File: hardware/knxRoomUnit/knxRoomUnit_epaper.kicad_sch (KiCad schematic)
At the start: 24 parts, among them P1 ePaper, P2 ePaper FL, Q3 SI1308

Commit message: Initial hardware commit
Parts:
- R30: renamed from R26; footprint Resistor_SMD:R_0402_1005Metric -> Resistor_SMD:R_0603_1608Metric
- R31: renamed from R27; footprint Resistor_SMD:R_0402_1005Metric -> Resistor_SMD:R_0603_1608Metric
- renumbered C24 to C20, C25 to C22, C20 to C23, C26 to C24, C27 to C25, C28 to C26, C22 to C27, C29 to C28, C23 to C29, P2 to P1, P1 to P2, R28 to R27, R29 to R28, R25 to R29

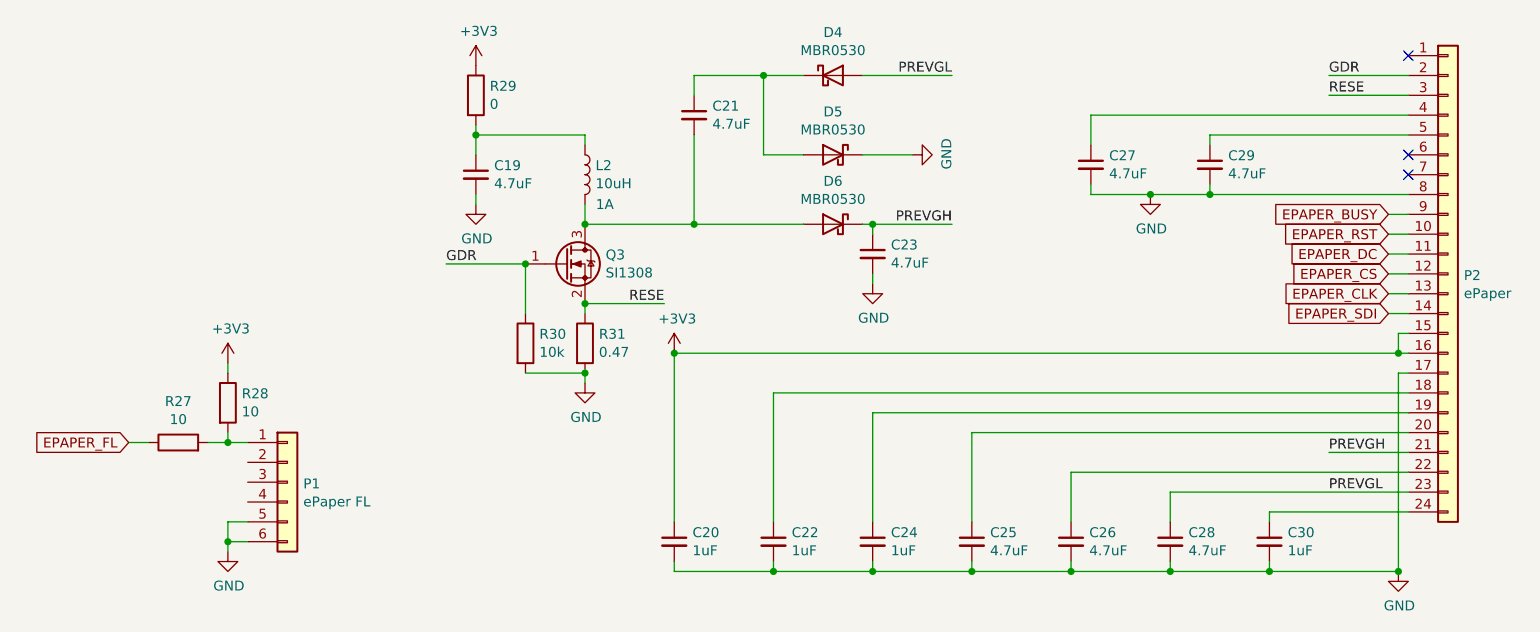
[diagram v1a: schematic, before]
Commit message: Updated sensors
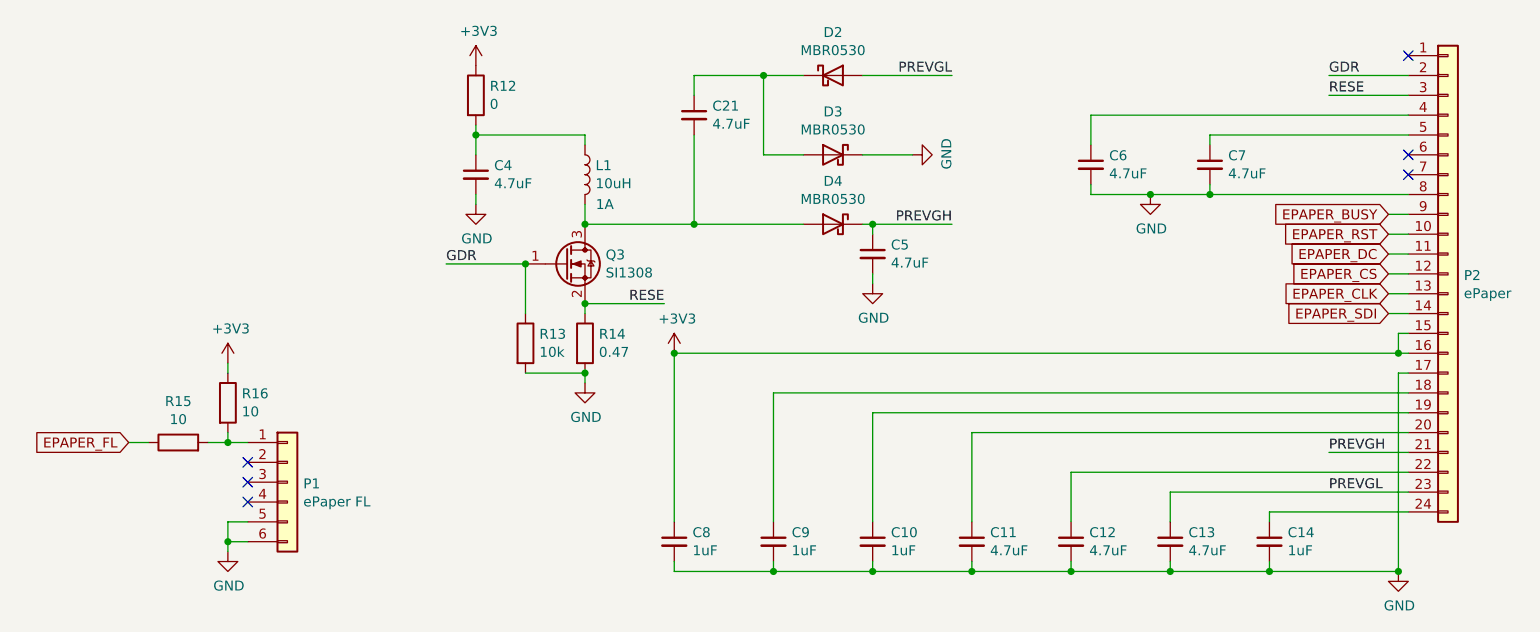
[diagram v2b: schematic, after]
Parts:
- renumbered C24 to C10, C25 to C11, C26 to C12, C28 to C13, C30 to C14, C19 to C4, C23 to C5, C27 to C6, C29 to C7, C20 to C8, C22 to C9, D4 to D2, D5 to D3, D6 to D4, L2 to L1, R29 to R12, R30 to R13, R31 to R14, R27 to R15, R28 to R16
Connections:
- no-connect marks 3 -> 6

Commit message: Production adjustments
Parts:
- D2, D3, D4: LCSC Part # C77336 -> C5204746; Manufacturer Changjiang Electronics Tech (CJ) -> TWGMC
- L1, P1, P2: now left out of the parts list
- R12, R15: Manufacturer Uniroyal Elec -> UNI-ROYAL(Uniroyal Elec)
- R13: LCSC Part # C25744 -> C25804; Manufacturer Uniroyal Elec -> UNI-ROYAL(Uniroyal Elec); PartNumber 0402WGF1002TCE -> 0603WAF1002T5E
- R16: LCSC Part # (none) -> C25278; Manufacturer (none) -> UNI-ROYAL(Uniroyal Elec); PartNumber (none) -> 0805W8J0100T5E; now left out of the parts list
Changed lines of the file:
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@@
   )
   (symbol (lib_id "Connector_Generic:Conn_01x24") (at 232.41 85.09 0) (unit 1)
-    (in_bom yes) (on_board yes) (dnp no)
+    (in_bom no) (on_board yes) (dnp no)
     (property "Reference" "P2" (at 234.442 85.2932 0)
       (effects (font (size 1.27 1.27)) (justify left))
@@
       (effects (font (size 1.27 1.27)) hide)
     )
-    (property "Datasheet" "https://datasheet.lcsc.com/lcsc/1810251812_Changjiang-Electronics-Tech-CJ-MBR0530_C77336.pdf" (at 153.67 59.69 0)
-      (effects (font (size 1.27 1.27)) hide)
-    )
-    (property "LCSC Part #" "C77336" (at 153.67 59.69 0)
-      (effects (font (size 1.27 1.27)) hide)
-    )
-    (property "Manufacturer" "Changjiang Electronics Tech (CJ)" (at 153.67 59.69 0)
+    (property "Datasheet" "https://datasheet.lcsc.com/lcsc/2210191600_TWGMC-MBR0530_C5204746.pdf" (at 153.67 59.69 0)
+      (effects (font (size 1.27 1.27)) hide)
+    )
+    (property "LCSC Part #" "C5204746" (at 153.67 59.69 0)
+      (effects (font (size 1.27 1.27)) hide)
+    )
+    (property "Manufacturer" "TWGMC" (at 153.67 59.69 0)
       (effects (font (size 1.27 1.27)) hide)
     )
@@
       (effects (font (size 1.27 1.27)) hide)
     )
-    (property "Datasheet" "https://datasheet.lcsc.com/lcsc/1810251812_Changjiang-Electronics-Tech-CJ-MBR0530_C77336.pdf" (at 153.67 69.85 0)
-      (effects (font (size 1.27 1.27)) hide)
-    )
-    (property "LCSC Part #" "C77336" (at 153.67 69.85 0)
-      (effects (font (size 1.27 1.27)) hide)
-    )
-    (property "Manufacturer" "Changjiang Electronics Tech (CJ)" (at 153.67 69.85 0)
+    (property "Datasheet" "https://datasheet.lcsc.com/lcsc/2210191600_TWGMC-MBR0530_C5204746.pdf" (at 153.67 69.85 0)
+      (effects (font (size 1.27 1.27)) hide)
+    )
+    (property "LCSC Part #" "C5204746" (at 153.67 69.85 0)
+      (effects (font (size 1.27 1.27)) hide)
+    )
+    (property "Manufacturer" "TWGMC" (at 153.67 69.85 0)
       (effects (font (size 1.27 1.27)) hide)
     )
@@
       (effects (font (size 1.27 1.27)) hide)
     )
-    (property "Datasheet" "https://datasheet.lcsc.com/lcsc/1810251812_Changjiang-Electronics-Tech-CJ-MBR0530_C77336.pdf" (at 153.67 78.74 0)
-      (effects (font (size 1.27 1.27)) hide)
-    )
-    (property "LCSC Part #" "C77336" (at 153.67 78.74 0)
-      (effects (font (size 1.27 1.27)) hide)
-    )
-    (property "Manufacturer" "Changjiang Electronics Tech (CJ)" (at 153.67 78.74 0)
+    (property "Datasheet" "https://datasheet.lcsc.com/lcsc/2210191600_TWGMC-MBR0530_C5204746.pdf" (at 153.67 78.74 0)
+      (effects (font (size 1.27 1.27)) hide)
+    )
+    (property "LCSC Part #" "C5204746" (at 153.67 78.74 0)
+      (effects (font (size 1.27 1.27)) hide)
+    )
+    (property "Manufacturer" "TWGMC" (at 153.67 78.74 0)
       (effects (font (size 1.27 1.27)) hide)
     )
@@
       (effects (font (size 1.27 1.27)) hide)
     )
-    (property "Datasheet" "https://datasheet.lcsc.com/lcsc/1809301717_UNI-ROYAL-Uniroyal-Elec-0402WGF1002TCE_C25744.pdf" (at 114.3 93.98 0)
-      (effects (font (size 1.27 1.27)) hide)
-    )
-    (property "LCSC Part #" "C25744" (at 114.3 93.98 0)
-      (effects (font (size 1.27 1.27)) hide)
-    )
-    (property "Manufacturer" "Uniroyal Elec" (at 114.3 93.98 0)
-      (effects (font (size 1.27 1.27)) hide)
-    )
-    (property "PartNumber" "0402WGF1002TCE" (at 114.3 93.98 0)
+    (property "Datasheet" "https://datasheet.lcsc.com/lcsc/2206010045_UNI-ROYAL-Uniroyal-Elec-0603WAF1002T5E_C25804.pdf" (at 114.3 93.98 0)
+      (effects (font (size 1.27 1.27)) hide)
+    )
+    (property "LCSC Part #" "C25804" (at 114.3 93.98 0)
+      (effects (font (size 1.27 1.27)) hide)
+    )
+    (property "Manufacturer" "UNI-ROYAL(Uniroyal Elec)" (at 114.3 93.98 0)
+      (effects (font (size 1.27 1.27)) hide)
+    )
+    (property "PartNumber" "0603WAF1002T5E" (at 114.3 93.98 0)
       (effects (font (size 1.27 1.27)) hide)
     )
@@
   )
   (symbol (lib_id "Device:L") (at 121.92 72.39 0) (unit 1)
-    (in_bom yes) (on_board yes) (dnp no)
+    (in_bom no) (on_board yes) (dnp no)
     (property "Reference" "L1" (at 123.2662 71.2216 0)
       (effects (font (size 1.27 1.27)) (justify left))
@@
       (effects (font (size 1.27 1.27)) hide)
     )
-    (property "Datasheet" "https://datasheet.lcsc.com/szlcsc/1912202016_Vishay-Intertech-SI1308EDL-T1-GE3_C469327.pdf" (at 119.38 83.82 0)
+    (property "Datasheet" "https://datasheet.lcsc.com/lcsc/1912202016_Vishay-Intertech-SI1308EDL-T1-GE3_C469327.pdf" (at 119.38 83.82 0)
       (effects (font (size 1.27 1.27)) hide)
     )
@@
       (effects (font (size 1.27 1.27)) hide)
     )
-    (property "Datasheet" "https://datasheet.lcsc.com/lcsc/1810271610_UNI-ROYAL-Uniroyal-Elec-0805W8F100JT5E_C17415.pdf" (at 69.85 106.68 0)
+    (property "Datasheet" "https://datasheet.lcsc.com/lcsc/2206010216_UNI-ROYAL-Uniroyal-Elec-0805W8F100JT5E_C17415.pdf" (at 69.85 106.68 0)
       (effects (font (size 1.27 1.27)) hide)
     )
@@
       (effects (font (size 1.27 1.27)) hide)
     )
-    (property "Manufacturer" "Uniroyal Elec" (at 69.85 106.68 0)
+    (property "Manufacturer" "UNI-ROYAL(Uniroyal Elec)" (at 69.85 106.68 0)
       (effects (font (size 1.27 1.27)) hide)
     )
@@
   )
   (symbol (lib_id "Connector_Generic:Conn_01x06") (at 83.82 111.76 0) (unit 1)
-    (in_bom yes) (on_board yes) (dnp no)
+    (in_bom no) (on_board yes) (dnp no)
     (property "Reference" "P1" (at 85.852 111.9632 0)
       (effects (font (size 1.27 1.27)) (justify left))
@@
   )
   (symbol (lib_id "Device:R") (at 76.2 101.6 0) (unit 1)
-    (in_bom yes) (on_board yes) (dnp no)
+    (in_bom no) (on_board yes) (dnp no)
     (property "Reference" "R16" (at 77.978 100.4316 0)
       (effects (font (size 1.27 1.27)) (justify left))
@@
       (effects (font (size 1.27 1.27)) hide)
     )
-    (property "Datasheet" "" (at 76.2 101.6 0)
-      (effects (font (size 1.27 1.27)) hide)
-    )
-    (property "LCSC Part #" "" (at 76.2 101.6 0)
-      (effects (font (size 1.27 1.27)) hide)
-    )
-    (property "Manufacturer" "" (at 76.2 101.6 0)
-      (effects (font (size 1.27 1.27)) hide)
-    )
-    (property "PartNumber" "" (at 76.2 101.6 0)
+    (property "Datasheet" "https://datasheet.lcsc.com/lcsc/2205311900_UNI-ROYAL-Uniroyal-Elec-0805W8J0100T5E_C25278.pdf" (at 76.2 101.6 0)
+      (effects (font (size 1.27 1.27)) hide)
+    )
+    (property "LCSC Part #" "C25278" (at 76.2 101.6 0)
+      (effects (font (size 1.27 1.27)) hide)
+    )
+    (property "Manufacturer" "UNI-ROYAL(Uniroyal Elec)" (at 76.2 101.6 0)
+      (effects (font (size 1.27 1.27)) hide)
+    )
+    (property "PartNumber" "0805W8J0100T5E" (at 76.2 101.6 0)
       (effects (font (size 1.27 1.27)) hide)
     )
@@
       (effects (font (size 1.27 1.27)) hide)
     )
-    (property "Datasheet" "https://datasheet.lcsc.com/szlcsc/Uniroyal-Elec-0805W8F0000T5E_C17477.pdf" (at 107.95 62.23 0)
+    (property "Datasheet" "https://datasheet.lcsc.com/lcsc/2206010216_UNI-ROYAL-Uniroyal-Elec-0805W8F0000T5E_C17477.pdf" (at 107.95 62.23 0)
       (effects (font (size 1.27 1.27)) hide)
     )
@@
       (effects (font (size 1.27 1.27)) hide)
     )
-    (property "Manufacturer" "Uniroyal Elec" (at 107.95 62.23 0)
-      (effects (font (size 1.27 1.27)) hide)
-    )
+    (property "Manufacturer" "UNI-ROYAL(Uniroyal Elec)" (at 107.95 62.23 0)
+      (effects (font (size 1.27 1.27)) hide)
+    )
